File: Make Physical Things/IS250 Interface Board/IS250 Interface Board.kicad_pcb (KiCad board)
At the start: 2 copper layers, 41 parts, among them J1 24_Pin_Reorg, J2 16_Pin, J3 Barrel_Jack, Q1 PN2222A, Q10 PN2222A, Q11 PN2907A, Q2 PN2907A, Q3 PN2222A, Q4 PN2222A, Q5 PN2222A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

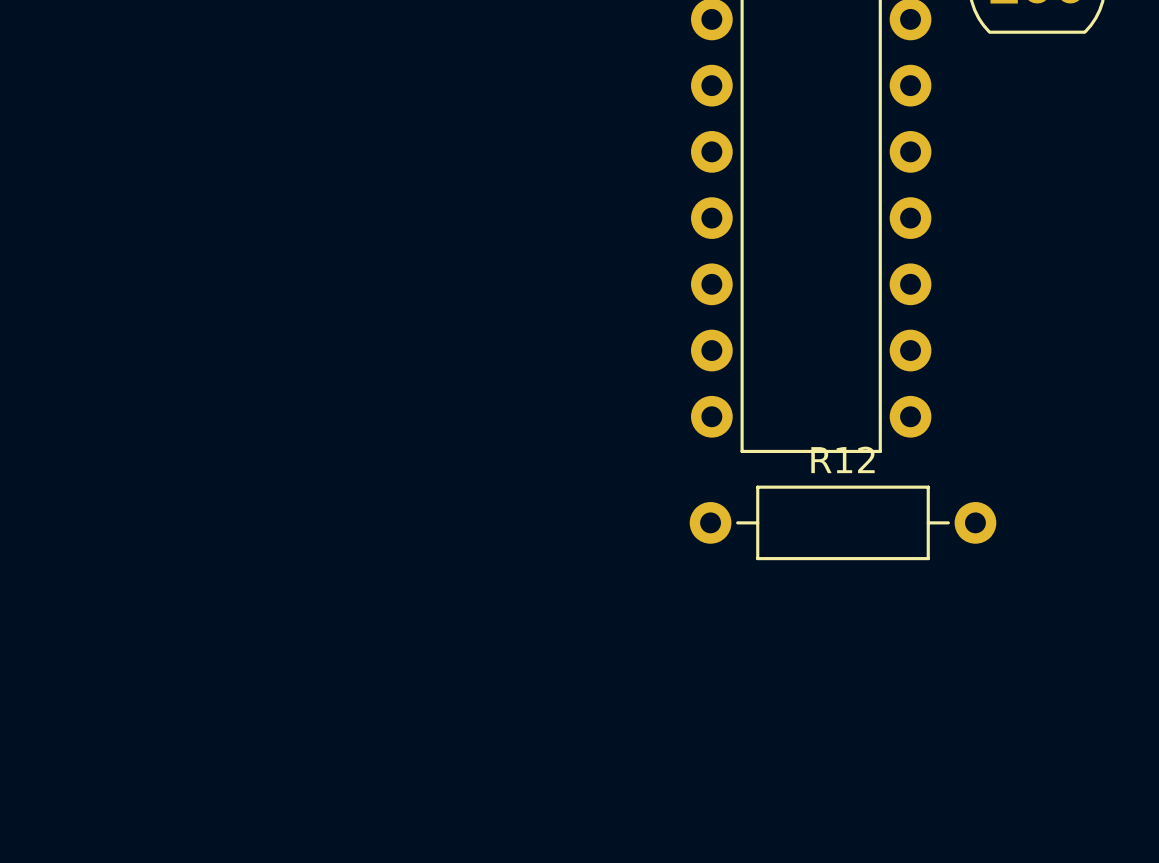
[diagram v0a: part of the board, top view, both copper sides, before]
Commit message: Added XT60 and backup fuel resistor
Added an XT60 power connector, and an optional resistor if there isn't an AD8400 connected, so that the fuel gauge will show not empty
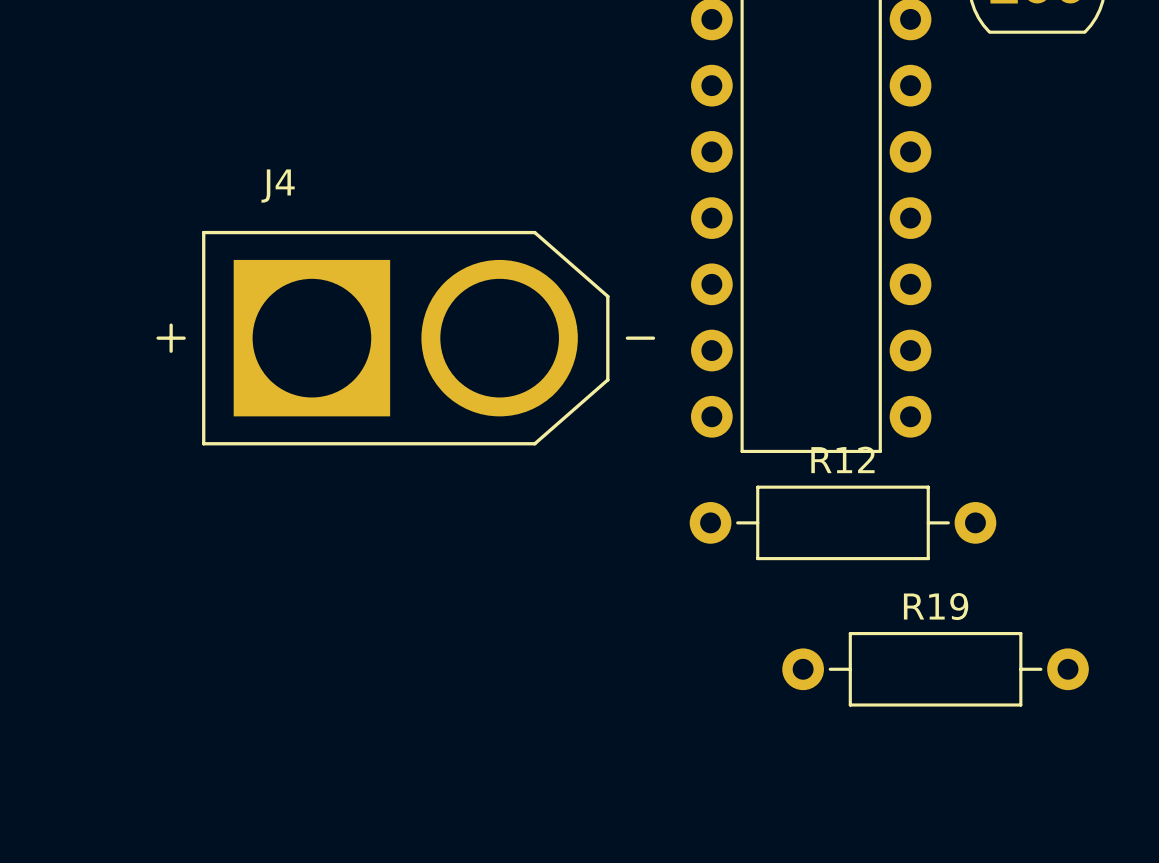
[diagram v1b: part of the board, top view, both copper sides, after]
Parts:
- added J4: XT60-M, XT60:AMASS_XT60-M, F.Cu at (251.5, 38.1)
- added R19: 100, Resistor_THT:R_Axial_DIN0207_L6.3mm_D2.5mm_P10.16mm_Horizontal, F.Cu at (266.7, 50.8)
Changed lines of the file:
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@@
     )
+  )
+  (footprint "XT60:AMASS_XT60-M" (layer "F.Cu")
+    (at 251.46 38.1)
+    (property "MANUFACTURER" "AMASS")
+    (property "MAXIMUM_PACKAGE_HEIGHT" "16.00 mm")
+    (property "PARTREV" "V1.2")
+    (property "STANDARD" "IPC 7351B")
+    (property "Sheetfile" "IS250 Interface Board.kicad_sch")
+    (property "Sheetname" "")
+    (attr through_hole)
+    (fp_text reference "J4" (at -4.825 -5.935) (layer "F.SilkS")
+      (effects (font (size 1 1) (thickness 0.15)))
+    )
+    (fp_text value "XT60-M" (at -0.38 5.935) (layer "F.Fab")
+      (effects (font (size 1 1) (thickness 0.15)))
+    )
+    (fp_line (start 8.5 0) (end 9.5 0) (layer "F.SilkS") (width 0.127))
+    (fp_line (start -9.5 0) (end -8.5 0) (layer "F.SilkS") (width 0.127))
+    (fp_line (start 4.95 4.05) (end -7.75 4.05) (layer "F.SilkS") (width 0.127))
+    (fp_line (start -7.75 -4.05) (end 4.95 -4.05) (layer "F.SilkS") (width 0.127))
+    (fp_line (start -9 -0.5) (end -9 0.5) (layer "F.SilkS") (width 0.127))
+    (fp_line (start 7.75 1.6) (end 4.95 4.05) (layer "F.SilkS") (width 0.127))
+    (fp_line (start 4.95 -4.05) (end 7.75 -1.6) (layer "F.SilkS") (width 0.127))
+    (fp_line (start -7.75 4.05) (end -7.75 -4.05) (layer "F.SilkS") (width 0.127))
+    (fp_line (start 7.75 -1.6) (end 7.75 1.6) (layer "F.SilkS") (width 0.127))
+    (fp_line (start -8 -4.3) (end -8 4.3) (layer "F.CrtYd") (width 0.05))
+    (fp_line (start 8 4.3) (end 8 -4.3) (layer "F.CrtYd") (width 0.05))
+    (fp_line (start 8 -4.3) (end -8 -4.3) (layer "F.CrtYd") (width 0.05))
+    (fp_line (start -8 4.3) (end 8 4.3) (layer "F.CrtYd") (width 0.05))
+    (fp_line (start 7.75 1.6) (end 4.95 4.05) (layer "F.Fab") (width 0.127))
+    (fp_line (start 8.5 0) (end 9.5 0) (layer "F.Fab") (width 0.127))
+    (fp_line (start -7.75 4.05) (end -7.75 -4.05) (layer "F.Fab") (width 0.127))
+    (fp_line (start 4.95 -4.05) (end 7.75 -1.6) (layer "F.Fab") (width 0.127))
+    (fp_line (start -9.5 0) (end -8.5 0) (layer "F.Fab") (width 0.127))
+    (fp_line (start 7.75 -1.6) (end 7.75 1.6) (layer "F.Fab") (width 0.127))
+    (fp_line (start 4.95 4.05) (end -7.75 4.05) (layer "F.Fab") (width 0.127))
+    (fp_line (start -7.75 -4.05) (end 4.95 -4.05) (layer "F.Fab") (width 0.127))
+    (fp_line (start -9 -0.5) (end -9 0.5) (layer "F.Fab") (width 0.127))
+    (pad "N" thru_hole circle locked (at 3.6 0) (size 6 6) (drill 4.55) (layers *.Cu *.Mask)
+      (net 1 "GND") (pinfunction "NEG") (pintype "passive"))
+    (pad "P" thru_hole rect locked (at -3.6 0) (size 6 6) (drill 4.55) (layers *.Cu *.Mask)
+      (net 22 "+12V") (pinfunction "POS") (pintype "passive"))
   )
   (footprint "Resistor_THT:R_Axial_DIN0207_L6.3mm_D2.5mm_P10.16mm_Horizontal" (layer "F.Cu")
@@
     (model "${KICAD6_3DMODEL_DIR}/Resistor_THT.3dshapes/R_Axial_DIN0207_L6.3mm_D2.5mm_P10.16mm_Horizontal.wrl"
       (offset (xyz 0 0 0))
+      (scale (xyz 1 1 1))
+      (rotate (xyz 0 0 0))
+    )
+  )
+  (footprint "Resistor_THT:R_Axial_DIN0207_L6.3mm_D2.5mm_P10.16mm_Horizontal" (layer "F.Cu")
+    (at 266.7 50.8)
+    (descr "Resistor, Axial_DIN0207 series, Axial, Horizontal, pin pitch=10.16mm, 0.25W = 1/4W, length*diameter=6.3*2.5mm^2, http://cdn-reichelt.de/documents/datenblatt/B400/1_4W%23YAG.pdf")
+    (tags "Resistor Axial_DIN0207 series Axial Horizontal pin pitch 10.16mm 0.25W = 1/4W length 6.3mm diameter 2.5mm")
+    (property "Sheetfile" "Fuel_System.kicad_sch")
+    (property "Sheetname" "Fuel System")
+    (attr through_hole)
+    (fp_text reference "R19" (at 5.08 -2.37) (layer "F.SilkS")
+      (effects (font (size 1 1) (thickness 0.15)))
+    )
+    (fp_text value "100" (at 5.08 2.37) (layer "F.Fab")
+      (effects (font (size 1 1) (thickness 0.15)))
+    )
+    (fp_text user "${REFERENCE}" (at 5.08 0) (layer "F.Fab")
+      (effects (font (size 1 1) (thickness 0.15)))
+    )
+    (fp_line (start 1.81 -1.37) (end 1.81 1.37) (layer "F.SilkS") (width 0.12))
+    (fp_line (start 1.04 0) (end 1.81 0) (layer "F.SilkS") (width 0.12))
+    (fp_line (start 1.81 1.37) (end 8.35 1.37) (layer "F.SilkS") (width 0.12))
+    (fp_line (start 9.12 0) (end 8.35 0) (layer "F.SilkS") (width 0.12))
+    (fp_line (start 8.35 1.37) (end 8.35 -1.37) (layer "F.SilkS") (width 0.12))
+    (fp_line (start 8.35 -1.37) (end 1.81 -1.37) (layer "F.SilkS") (width 0.12))
+    (fp_line (start 11.21 1.5) (end 11.21 -1.5) (layer "F.CrtYd") (width 0.05))
+    (fp_line (start -1.05 -1.5) (end -1.05 1.5) (layer "F.CrtYd") (width 0.05))
+    (fp_line (start -1.05 1.5) (end 11.21 1.5) (layer "F.CrtYd") (width 0.05))
+    (fp_line (start 11.21 -1.5) (end -1.05 -1.5) (layer "F.CrtYd") (width 0.05))
+    (fp_line (start 8.23 -1.25) (end 1.93 -1.25) (layer "F.Fab") (width 0.1))
+    (fp_line (start 1.93 1.25) (end 8.23 1.25) (layer "F.Fab") (width 0.1))
+    (fp_line (start 10.16 0) (end 8.23 0) (layer "F.Fab") (width 0.1))
+    (fp_line (start 0 0) (end 1.93 0) (layer "F.Fab") (width 0.1))
+    (fp_line (start 8.23 1.25) (end 8.23 -1.25) (layer "F.Fab") (width 0.1))
+    (fp_line (start 1.93 -1.25) (end 1.93 1.25) (layer "F.Fab") (width 0.1))
+    (pad "1" thru_hole circle (at 0 0) (size 1.6 1.6) (drill 0.8) (layers *.Cu *.Mask)
+      (net 2 "/Fuel System/FUEL-GND") (pintype "passive"))
+    (pad "2" thru_hole oval (at 10.16 0) (size 1.6 1.6) (drill 0.8) (layers *.Cu *.Mask)
+      (net 18 "/Fuel System/FUEL") (pintype "passive"))
+    (model "${KICAD6_3DMODEL_DIR}/Resistor_THT.3dshapes/R_Axial_DIN0207_L6.3mm_D2.5mm_P10.16mm_Horizontal.wrl"
+      (offset (xyz 0 0 0))

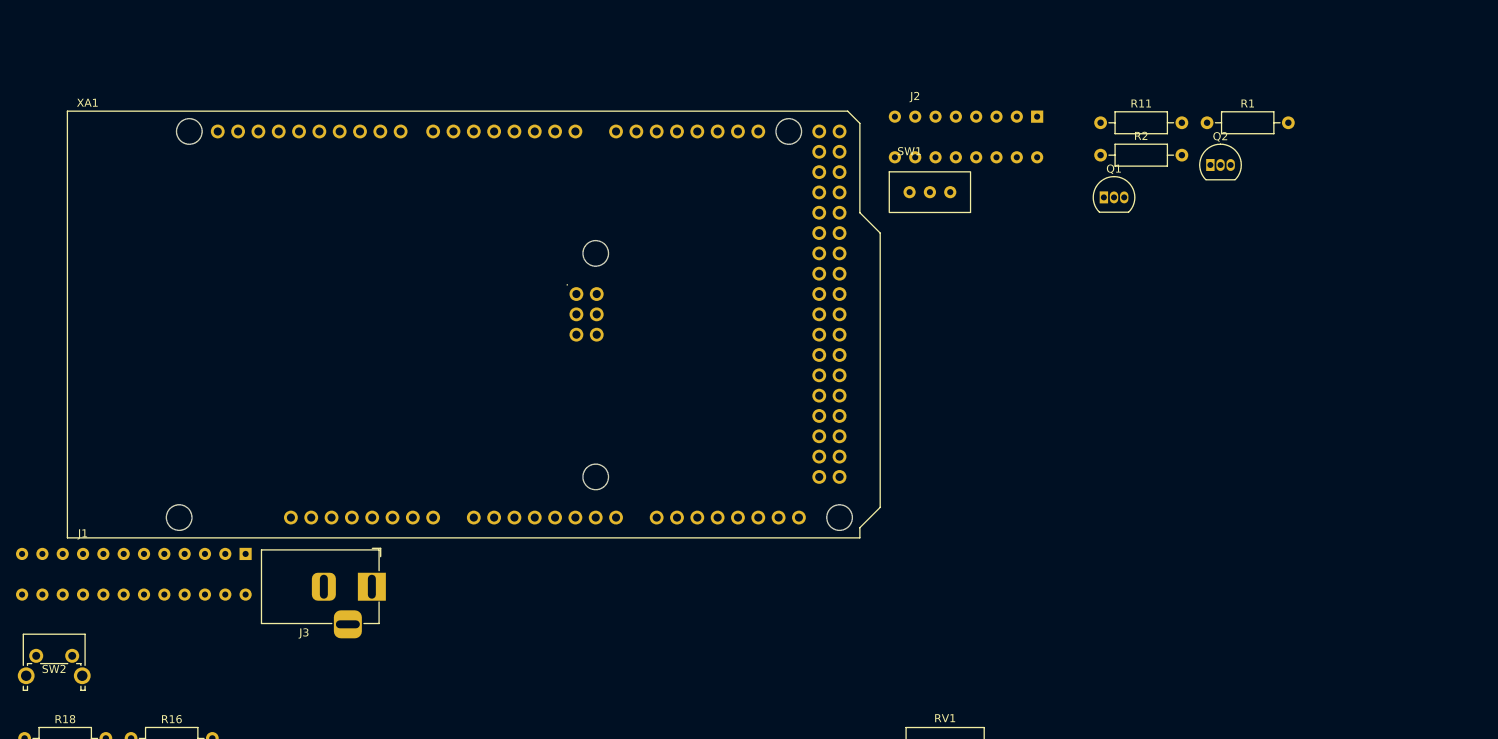
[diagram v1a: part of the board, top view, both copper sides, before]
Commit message: Added Reset Circuit
Added a button to allow you to reset the arduino, if it decides to die. Also fixed the footprints for the buttons so that they actually function as buttons.
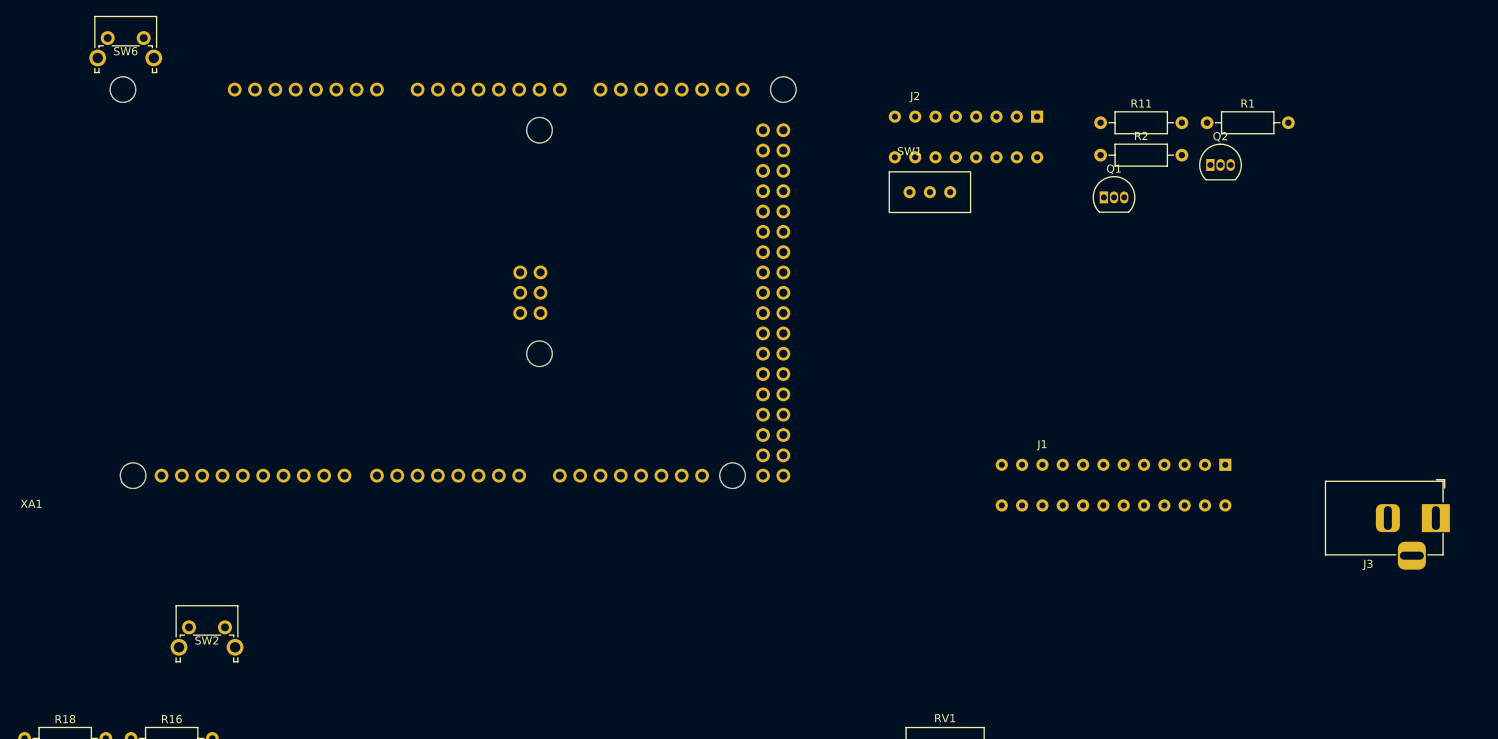
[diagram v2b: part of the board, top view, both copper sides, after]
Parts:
- added SW6: SW_MEC_5G, Button_Switch_THT:SW_Tactile_SPST_Angled_PTS645Vx58-2LFS, F.Cu at (27.9, 12.7)
- XA1: moved to B.Cu
- moved J3 133.3 mm to (194.0, 72.7)
- moved J1 123.0 mm to (152.4, 68.6)
- moved XA1 59.0 mm to (15.9, 16.6)
- moved SW2 19.4 mm to (38.1, 86.4)
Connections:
- SW2 pad 1: Net-(J1-Pad20) -> GND
- SW2 pad 2: Net-(J1-Pad20) -> GND
- SW3 pad 1: /Satellite Switch/RSEL -> GND
- SW4 pad 1: /Satellite Switch/SET -> GND
- SW5 pad 1: /Satellite Switch/LSEL -> GND
- XA1 pad D42: unconnected-(XA1-PadD42) -> /Tacho
- XA1 pad D43: unconnected-(XA1-PadD43) -> /Speedo
- XA1 pad D44: /Tacho -> unconnected-(XA1-PadD44)
- XA1 pad D45: /Speedo -> unconnected-(XA1-PadD45)
- XA1 pad RST1: unconnected-(XA1-PadRST1) -> Net-(XA1-PadRST1)

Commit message: Added Power LED's and PCB foundation
Added LED's to indicate both 12v and 5v power to the board, and begun work on the PCB
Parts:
- added D1: LED, LED_THT:LED_D5.0mm, F.Cu at (225.4, 170.7)
- added D2: LED, LED_THT:LED_D5.0mm, F.Cu at (236.2, 162.6)
- added R20: 2k, Resistor_THT:R_Axial_DIN0207_L6.3mm_D2.5mm_P10.16mm_Horizontal, F.Cu at (222.0, 164.9)
- added R21: 1k, Resistor_THT:R_Axial_DIN0207_L6.3mm_D2.5mm_P10.16mm_Horizontal, F.Cu at (222.0, 160.8)
- moved R16 131.3 mm to (162.2, 96.3)
- moved Q10 131.3 mm to (149.2, 105.7)
- moved Q11 131.3 mm to (162.6, 101.6)
- moved R17 131.3 mm to (148.8, 100.4)
- moved R18 131.3 mm to (148.8, 96.3)
- moved SW3 129.1 mm to (139.7, 20.3)
- moved J4 116.1 mm to (271.8, 152.4)
- moved SW4 109.5 mm to (152.4, 20.3)
- moved SW5 107.1 mm to (165.1, 20.3)
- moved SW2 106.7 mm to (121.9, 20.3)
- moved RV1 101.7 mm to (221.0, 55.9), turned to -90 degrees
- moved J3 101.3 mm to (256.5, 152.4)
- moved J1 86.4 mm to (228.6, 27.9)
- moved Q8 86.3 mm to (136.6, 80.2)
- moved R14 86.3 mm to (136.1, 75.0)
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
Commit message: More PCB Layout
PCB laid out further, and just requires routing and silkscreen.
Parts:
- moved R9 202.9 mm to (215.9, 68.6), turned to -90 degrees
- moved J4 197.0 mm to (75.1, 139.7), turned to 180 degrees
- moved R10 187.5 mm to (210.8, 68.6), turned to -90 degrees
- moved Q6 179.6 mm to (213.4, 88.9)
- moved J3 179.2 mm to (79.7, 123.5)
- moved R20 138.4 mm to (88.9, 127.0)
- moved Q4 135.5 mm to (142.2, 124.5), turned to -90 degrees
- moved R21 135.2 mm to (88.9, 137.2)
- moved R8 135.1 mm to (147.3, 119.4), turned to 180 degrees
- moved R5 132.9 mm to (144.8, 134.6)
- moved D2 132.0 mm to (106.7, 137.2), turned to 180 degrees
- moved R7 129.0 mm to (167.6, 119.4), turned to 180 degrees
- moved D1 126.5 mm to (106.7, 127.0), turned to 180 degrees
- moved R4 124.7 mm to (139.7, 139.7)
- moved Q5 122.2 mm to (150.7, 119.4)
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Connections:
- SW2 pad 1: GND -> Net-(J1-Pad20)
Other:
- board outline added: 175.3 x 106.7 mm

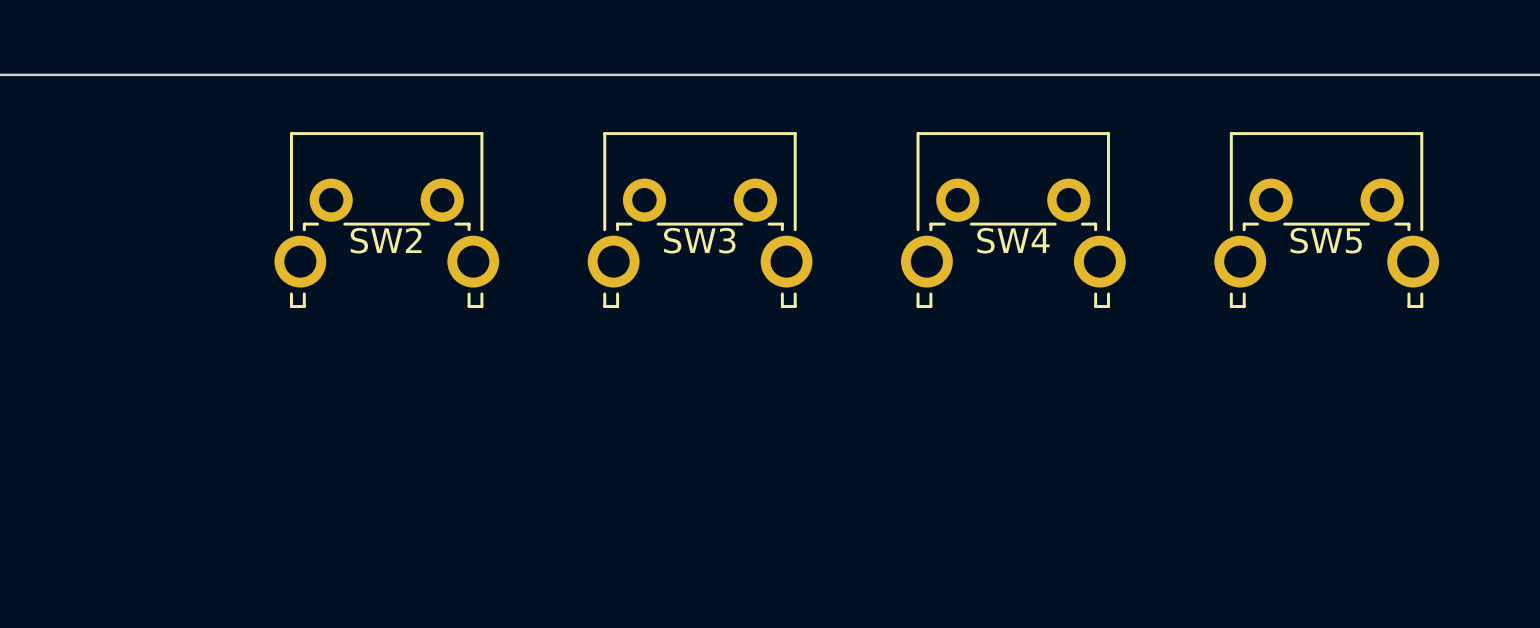
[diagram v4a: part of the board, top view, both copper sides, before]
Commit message: PCB Layout Finalised
Finalised the layout, routing and silkscreen still to be completed.
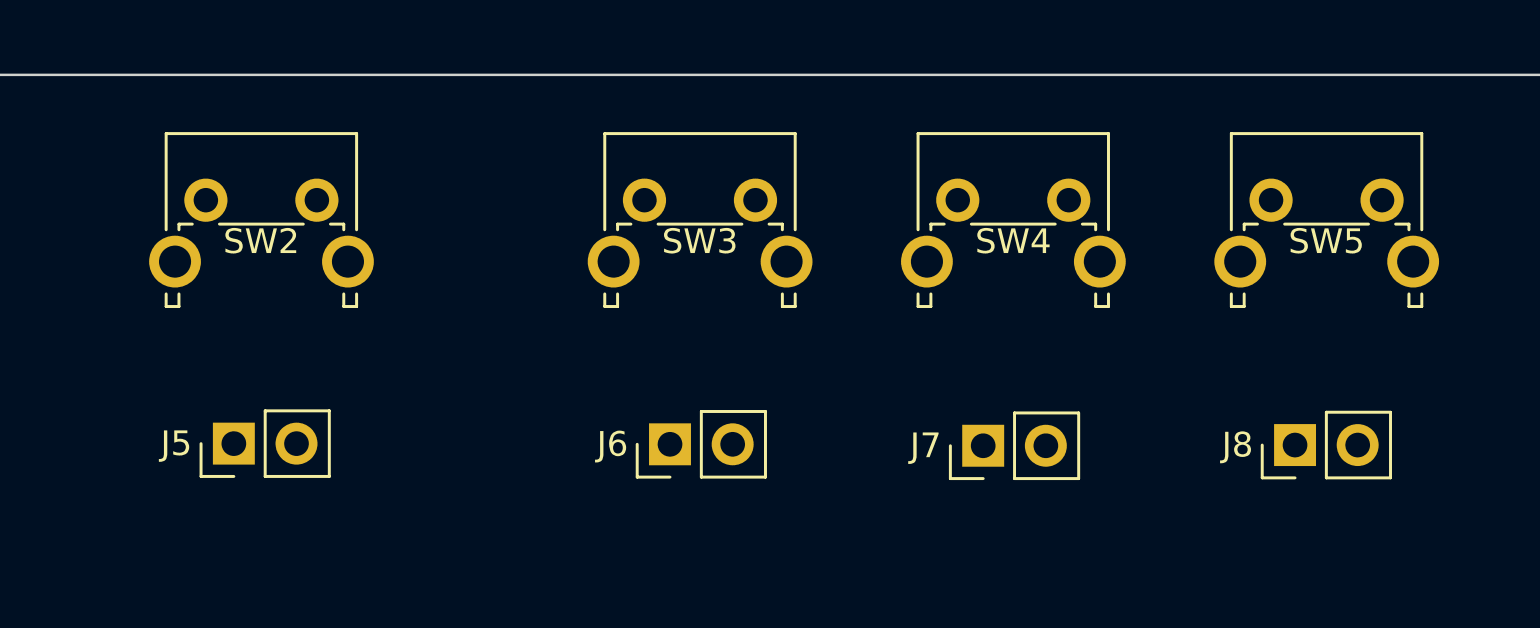
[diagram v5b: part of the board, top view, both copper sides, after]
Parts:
- added J5: Conn_01x02, Connector_PinHeader_2.54mm:PinHeader_1x02_P2.54mm_Vertical, F.Cu at (87.5, 55.6)
- added J6: Conn_01x02, Connector_PinHeader_2.54mm:PinHeader_1x02_P2.54mm_Vertical, F.Cu at (105.2, 55.6)
- added J7: Conn_01x02, Connector_PinHeader_2.54mm:PinHeader_1x02_P2.54mm_Vertical, F.Cu at (117.9, 55.7)
- added J8: Conn_01x02, Connector_PinHeader_2.54mm:PinHeader_1x02_P2.54mm_Vertical, F.Cu at (130.5, 55.6)
- moved SW2 5.08 mm to (86.4, 45.7)
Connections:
- XA1 pad GND6: unconnected-(XA1-PadGND6) -> GND
